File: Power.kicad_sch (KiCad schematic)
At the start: 60 parts, among them J11 Conn_01x02, J12 Conn_01x02, J4 Conn_01x02, J5 Conn_01x02, U10 NCV8170AXV300T2G, U12 R5478N101CD, U13 FDV301N, U14 FDV301N, U15 R5478N101CD, U16 FDV301N, U17 FDV301N, U26 NCV8170BXV180T2G, U28 BSS138L, U3 Conn_01x04, U30 BSS138L, U31 BSS138L, U33 NCV8170AXV300T2G, U9 MCP73831-2-OT

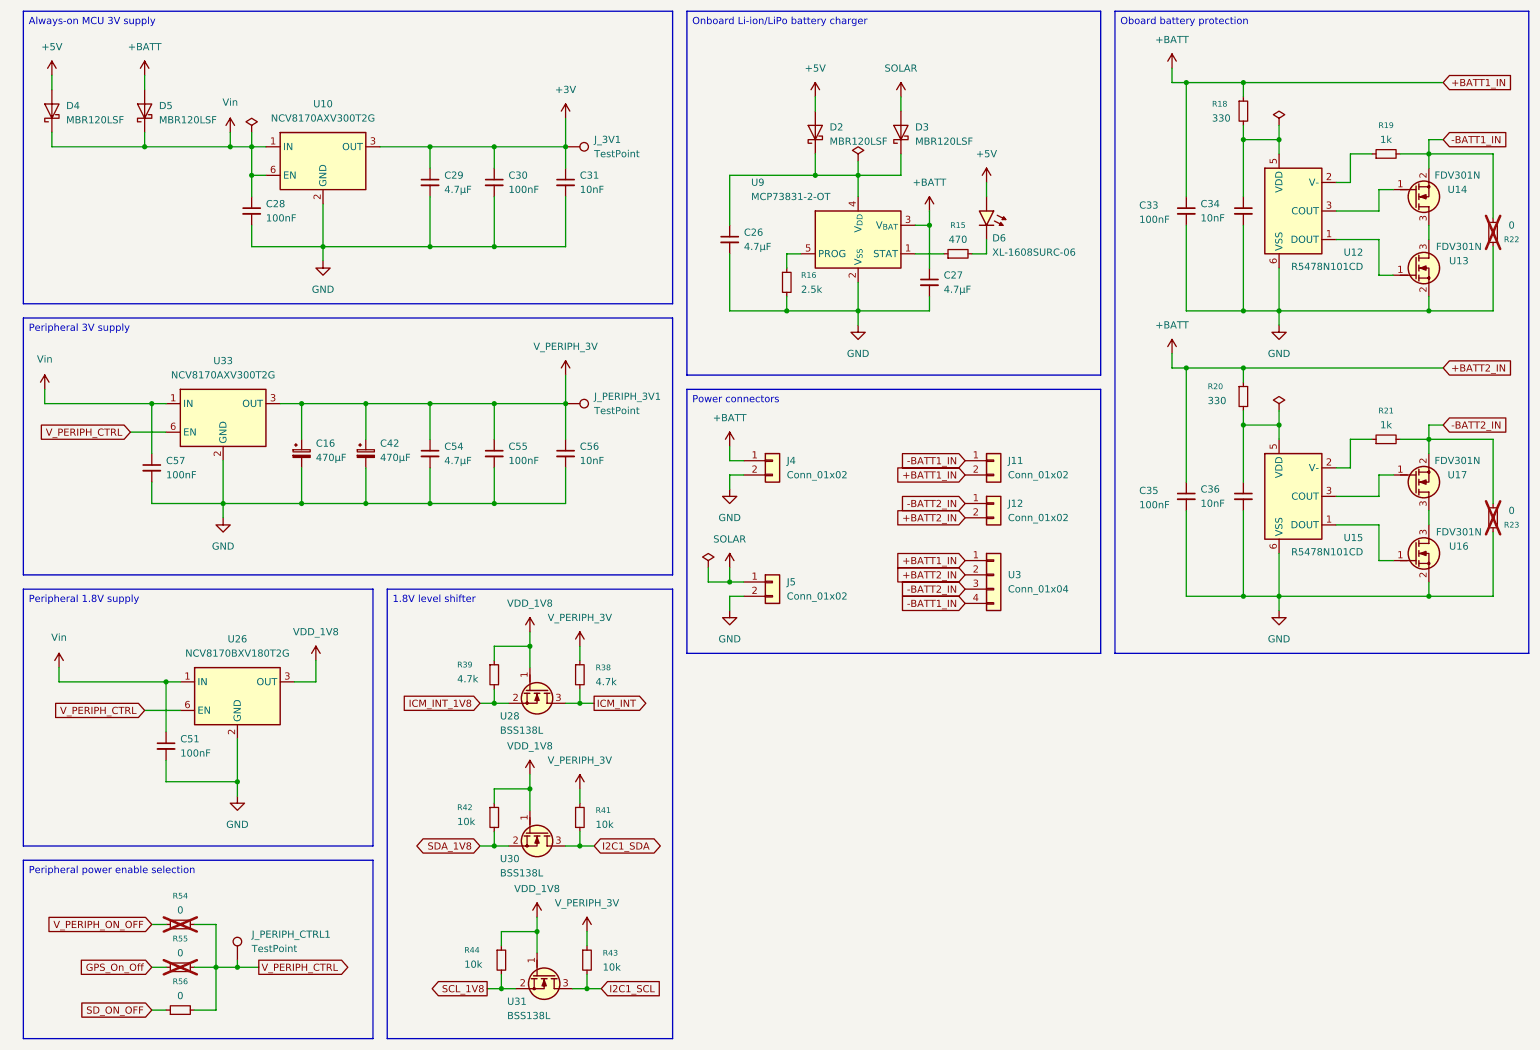
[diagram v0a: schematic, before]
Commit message: WIP: remove unneeded parts from PCB, add SPA06 and FHTC3 to schematics
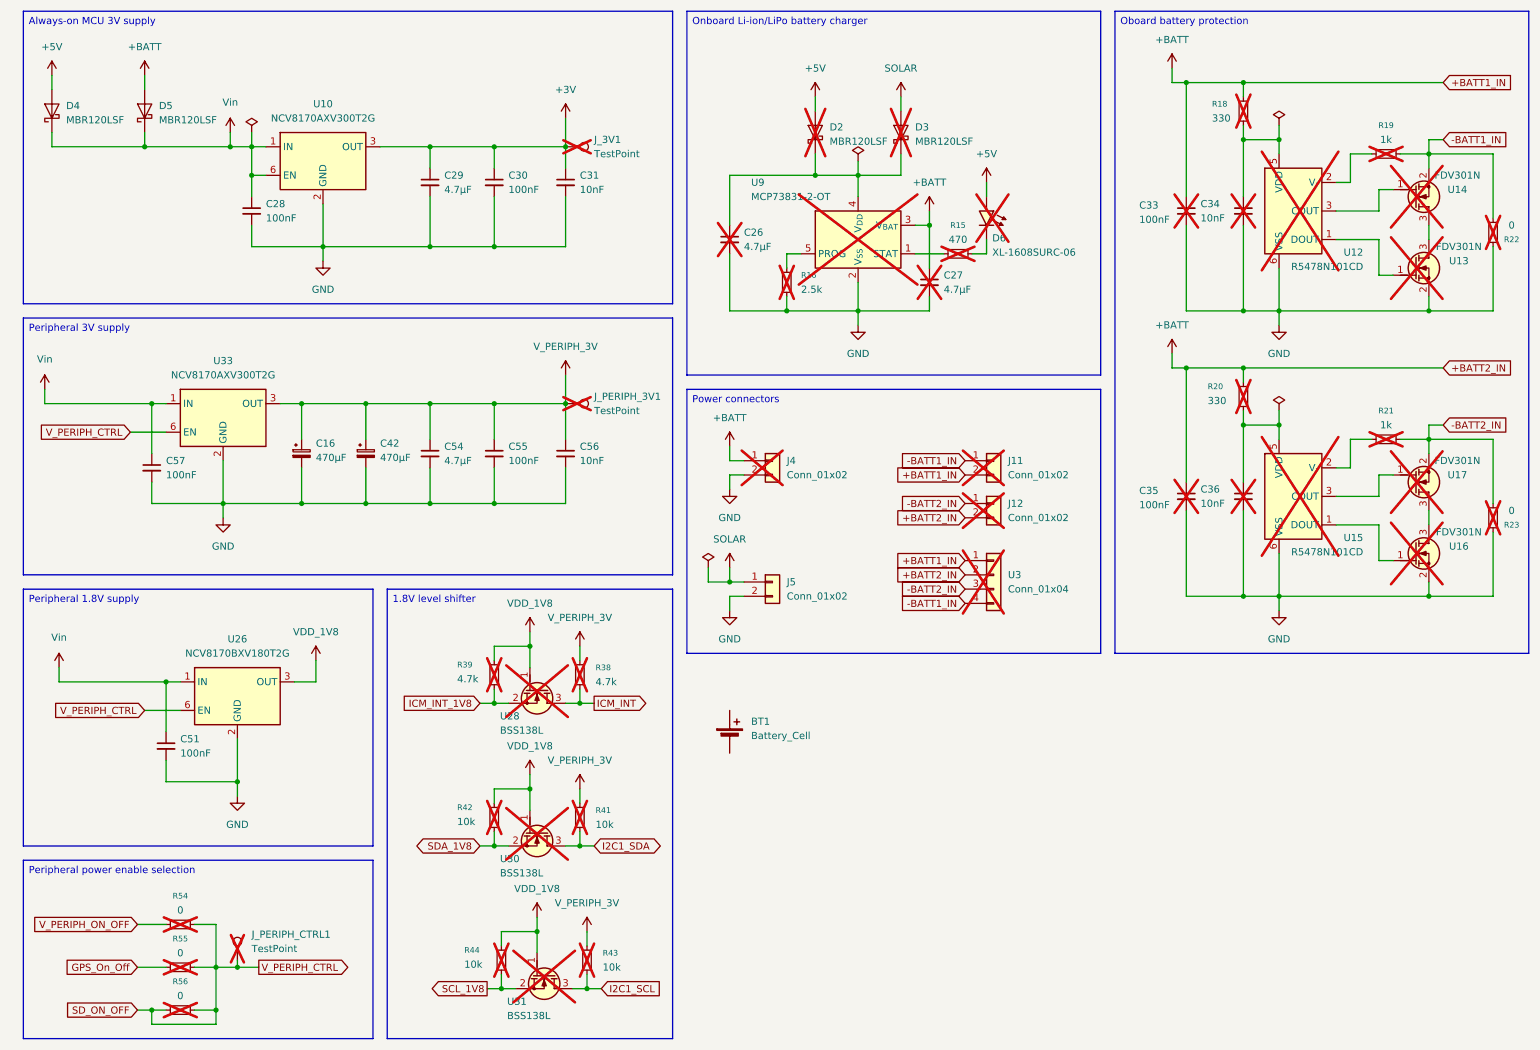
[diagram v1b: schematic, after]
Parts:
- added BT1: Battery_Cell, Battery:BatteryHolder_MPD_BK-18650-PC2, symbol Device:Battery_Cell
- C26, C27, C33, C34, C35, C36, D2, D3, D6, J11, J12, J4, J_3V1, J_PERIPH_3V1, J_PERIPH_CTRL1, R15, R16, R18, R19, R20, R21, R38, R39, R41, R42, R43, R44, R56, U12, U13, U14, U15, U16, U17, U28, U3, U30, U31, U9: now not fitted; now left out of the parts list
- R22, R23: now left out of the parts list
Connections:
- net V_PERIPH_CTRL is gone; now on net SD_ON_OFF: J_PERIPH_CTRL1.1, R54.2, R55.2, R56.2, U26.6 (EN), U33.6 (EN)

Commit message: WIP: import ambient-pcb-lifepo4protection and ambient-pcb-audiopower schematics
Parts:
- removed BT1: Battery_Cell, Battery:BatteryHolder_MPD_BK-18650-PC2, symbol Device:Battery_Cell
- added JP10, JP11: Jumper_2_Bridged, Jumper:SolderJumper-2_P1.3mm_Bridged2Bar_Pad1.0x1.5mm, symbol Jumper:SolderJumper_2_Bridged
- C26, C27, C33, C34, C35, C36: now in the parts list
- D4, D5: now not fitted; now left out of the parts list
- U3: footprint footprints:BAT-TH_BH-18650-A1BJ034 -> Connector_PinHeader_2.54mm:PinHeader_1x04_P2.54mm_Vertical
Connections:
- net Vin is gone; now on net +BATT: C28.1, C51.1, C57.1, D4.1 (K), D5.1 (K), U10.1 (IN), U10.6 (EN), U26.1 (IN), U33.1 (IN)
- net +BATT: now also JP10.1 (A), JP11.1 (A); no longer J11.2 (Pin_2), J12.2 (Pin_2), U3.1 (Pin_1), U3.2 (Pin_2)
- net VDD_1V8 renamed +1V8
- net V_PERIPH_3V renamed +3V0_PERIPH
- new net +BATT1_IN: J11.2 (Pin_2), JP10.2 (B), U3.1 (Pin_1)
- new net +BATT2_IN: J12.2 (Pin_2), JP11.2 (B), U3.2 (Pin_2)
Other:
- moved on the sheet: C16, C28, C29, C30, C31, C42, C54, C55, C56, C57, J_3V1, J_PERIPH_3V1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

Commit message: WIP: BOM
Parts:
- removed U10, U33: NCV8170AXV300T2G, Package_TO_SOT_SMD:SOT-563, symbol Onsemi_NCV8170:NCV8170AXV300T2G
- removed U26: NCV8170BXV180T2G, Package_TO_SOT_SMD:SOT-563, symbol Onsemi_NCV8170:NCV8170BXV180T2G
- added C116: 4.7µF, Capacitor_SMD:C_0402_1005Metric, symbol Device:C_Small
- added C117: 820µF, Capacitor_SMD:CP_Elec_6.3x9.9, symbol Device:C_Polarized_Small
- added R114: 4.7k, Resistor_SMD:R_0402_1005Metric, symbol Device:R_Small
- added U10, U33, U46: RT9080-30GJ5, Package_TO_SOT_SMD:TSOT-23-5, symbol RT9080-30GJ5:RT9080-30GJ5
- added U47: RT9080-18GJ5, Package_TO_SOT_SMD:TSOT-23-5, symbol RT9080-30GJ5:RT9080-30GJ5
- C16, C42: LCSC (none) -> C402828; now not fitted; now left out of the parts list
- C26, C27: LCSC (none) -> C23733; now left out of the parts list
- C28, C30, C51, C55, C57: LCSC (none) -> C1525
- C29, C54: LCSC (none) -> C23733
- C31, C56: LCSC (none) -> C15195; now not fitted; now left out of the parts list
- C33, C35: LCSC (none) -> C1525; now left out of the parts list
- C34, C36: LCSC (none) -> C15195; now left out of the parts list
- J11, J12, J5: footprint Connector_PinHeader_2.54mm:PinHeader_1x02_P2.54mm_Vertical -> Connector_JST:JST_XH_B2B-XH-A_1x02_P2.50mm_Vertical; LCSC (none) -> C20079
- J4: footprint Connector_PinSocket_2.54mm:PinSocket_1x02_P2.54mm_Vertical -> Connector_JST:JST_XH_B2B-XH-A_1x02_P2.50mm_Vertical; LCSC (none) -> C20079
- R15: LCSC (none) -> C25117
- R16: value 2.5k -> 2.2k; LCSC (none) -> C25879
- R18, R20: LCSC (none) -> C25104
- R19, R21: LCSC (none) -> C11702
- R22, R23, R54, R55, R56: LCSC (none) -> C17168
- R38, R39: LCSC (none) -> C25900
- R41, R42, R43, R44: LCSC (none) -> C25744
- U12, U15: LCSC (none) -> C259800
- U13, U14, U16, U17: LCSC (none) -> C20069151
- U28, U30, U31: LCSC (none) -> C5224261
- U3: footprint Connector_PinHeader_2.54mm:PinHeader_1x04_P2.54mm_Vertical -> Connector_JST:JST_XH_B4B-XH-A_1x04_P2.50mm_Vertical; LCSC (none) -> C37815
- U9: LCSC C14879 -> C32574
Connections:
- net +1V8: now also U47.5 (VOUT)
- net +3V: now also U10.5 (VOUT)
- net +3V0_PERIPH: now also C117.1, U33.5 (VOUT)
- net +BATT: now also U10.1 (VIN), U10.3 (EN), U33.1 (VIN), U46.1 (VIN), U47.1 (VIN)
- net GND: now also C116.2, C117.2, R114.2, U10.2 (GND), U33.2 (GND), U46.2 (GND), U47.2 (GND)
- net SD_ON_OFF: now also R114.1, U46.3 (EN); no longer J_PERIPH_CTRL1.1, R54.2, R55.2, R56.2
- net V_PERIPH_ON_OFF renamed V_PERIPH_CTRL
- net V_PERIPH_CTRL: now also J_PERIPH_CTRL1.1, R54.2, R55.2, R56.2, U33.3 (EN), U47.3 (EN)
- new net +3V0_SD: C116.1, U46.5 (VOUT)
- no-connect marks 0 -> 3
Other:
- moved on the sheet: C26, C27, C28, C51, C54, C55, C57, D2, D3, D6, J11, J12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

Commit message: WIP: omit some components and perform initial rough placement on PCB
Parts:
- added C110, C120, C79: 4.7µF, Capacitor_SMD:C_0402_1005Metric, symbol Device:C_Small
- added C121: 47µF/10V, Capacitor_SMD:C_1206_3216Metric, symbol Device:C_Small
- R54, R55: now left out of the parts list
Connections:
- net +1V8: now also C79.1
- net +BATT: now also C110.1, C120.1, C121.1
- net GND: now also C110.2, C120.2, C121.2, C79.2
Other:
- moved on the sheet: C117, C16, C42, C51, C54, C55, C56, C57, J_PERIPH_3V1, U33, U47

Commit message: WIP: start routing
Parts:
- J5: now not fitted; now left out of the parts list
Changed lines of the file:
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@@
 		(body_style 1)
 		(exclude_from_sim no)
-		(in_bom yes)
-		(on_board yes)
-		(in_pos_files yes)
-		(dnp no)
+		(in_bom no)
+		(on_board no)
+		(in_pos_files no)
+		(dnp yes)
 		(fields_autoplaced yes)
 		(property "Reference" "J5"
@@
 					(variant
 						(name "Ambient")
-						(dnp yes)
+						(in_bom yes)
+						(on_board yes)
+						(in_pos_files yes)
 					)
 				)
